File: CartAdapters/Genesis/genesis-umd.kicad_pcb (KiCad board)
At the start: 2 copper layers, 26.7 x 94.6 mm, 4 parts, among them CON101 UMDv2-CONN, CON102 GENESIS-CONN, U101 MCP23008T-E_SS

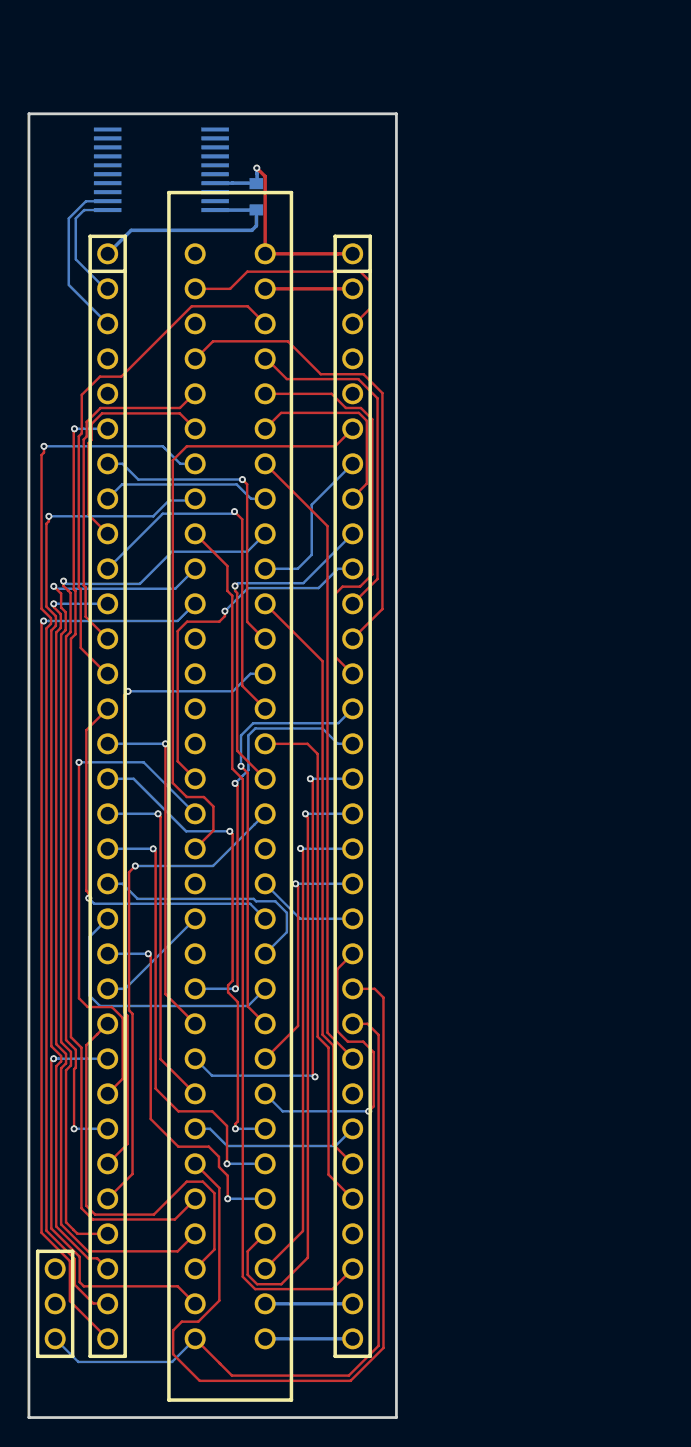
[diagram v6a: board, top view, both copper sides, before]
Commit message: ground plane added to genesis UMD adapter
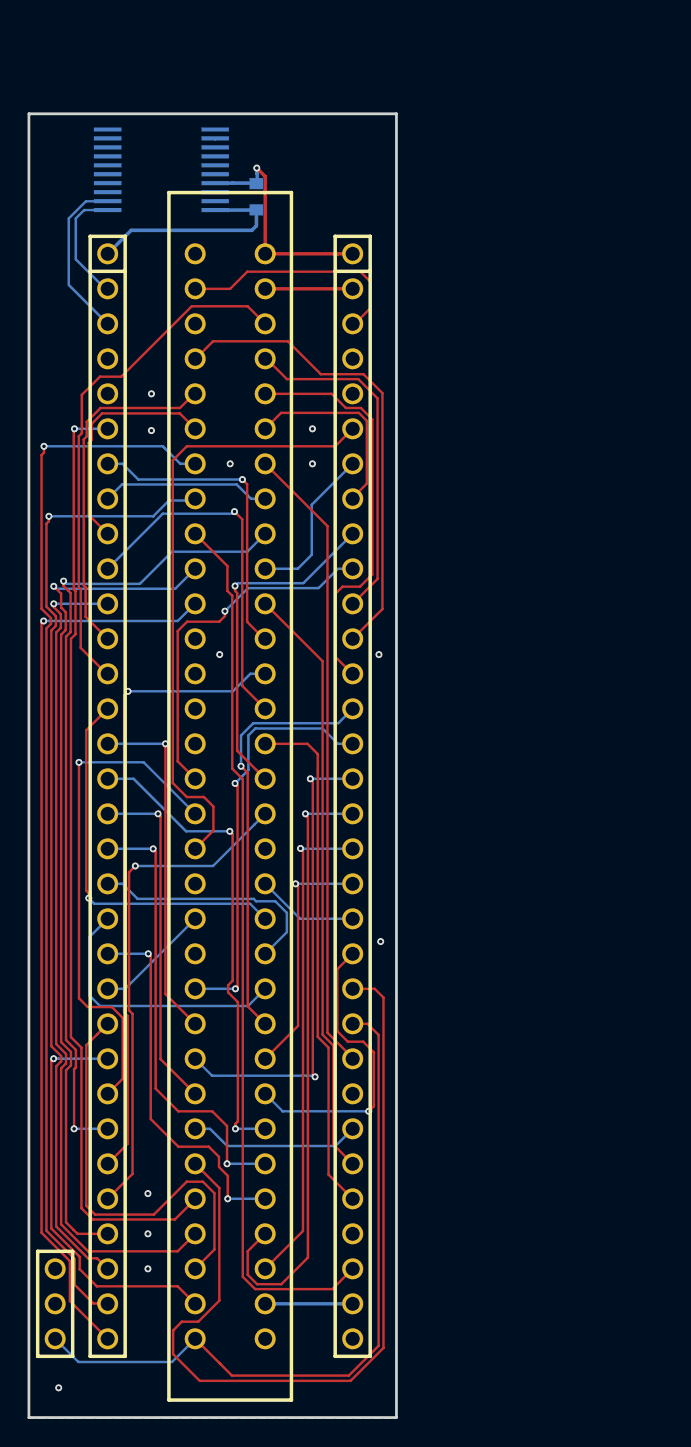
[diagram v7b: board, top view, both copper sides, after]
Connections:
- CON101 pad 33: /GND_1 -> GND
- CON102 pad A18: Net-(CON102-PadA18) -> GND
- CON102 pad A32: /GND_1 -> GND
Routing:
- net /GND_1: track 6.35 -> 0.00 mm
- net /~TIME~: track 30.1 -> 29.6 mm
- net GND: vias 1 -> 13
- added copper zone on B.Cu, net GND
- added copper zone on F.Cu, net GND
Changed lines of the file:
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@@
     (thickness 1.6)
     (drawings 4)
-    (tracks 489)
+    (tracks 501)
     (zones 0)
     (modules 4)
-    (nets 80)
+    (nets 78)
   )
   (page A4)
@@
     (35 F.Paste user)
     (36 B.SilkS user)
-    (37 F.SilkS user hide)
+    (37 F.SilkS user)
     (38 B.Mask user)
     (39 F.Mask user)
@@
     (last_trace_width 0.1778)
     (trace_clearance 0.1778)
-    (zone_clearance 0.508)
+    (zone_clearance 0.254)
     (zone_45_only no)
     (trace_min 0.1778)
@@
   (net 76 /5V_0)
   (net 77 /5V_1)
-  (net 78 /GND_1)
-  (net 79 "Net-(CON102-PadA18)")
   (net_class Default "This is the default net class."
     (clearance 0.1778)
@@
     (add_net /D8)
     (add_net /D9)
-    (add_net /GND_1)
     (add_net /SCL)
     (add_net /SDA)
@@
     (add_net "Net-(CON101-Pad65)")
     (add_net "Net-(CON101-Pad66)")
-    (add_net "Net-(CON102-PadA18)")
     (add_net "Net-(CON102-PadB1)")
     (add_net "Net-(CON102-PadB12)")
@@
       (net 77 /5V_1))
     (pad 33 thru_hole circle (at 17.78 78.74) (size 1.524 1.524) (drill 1.016) (layers *.Cu *.Mask)
-      (net 78 /GND_1))
+      (net 2 GND))
     (pad 32 thru_hole circle (at 0 78.74) (size 1.524 1.524) (drill 1.016) (layers *.Cu *.Mask)
       (net 29 /A23))
@@
       (net 46 /D1))
     (pad A32 thru_hole circle (at 5.08 78.74 180) (size 1.524 1.524) (drill 1.016) (layers *.Cu *.Mask)
-      (net 78 /GND_1))
+      (net 2 GND))
     (pad A31 thru_hole circle (at 5.08 76.2 180) (size 1.524 1.524) (drill 1.016) (layers *.Cu *.Mask)
       (net 77 /5V_1))
@@
       (net 25 /A1))
     (pad A18 thru_hole circle (at 5.08 43.18 180) (size 1.524 1.524) (drill 1.016) (layers *.Cu *.Mask)
-      (net 79 "Net-(CON102-PadA18)"))
+      (net 2 GND))
     (pad A19 thru_hole circle (at 5.08 45.72 180) (size 1.524 1.524) (drill 1.016) (layers *.Cu *.Mask)
       (net 40 /D7))
@@
   (segment (start 144.9498 60.9092) (end 146.6342 60.9092) (width 0.254) (layer B.Cu) (net 2))
   (segment (start 146.6342 60.9092) (end 146.6596 60.8838) (width 0.254) (layer B.Cu) (net 2))
-  (segment (start 147.32 144.78) (end 153.67 144.78) (width 0.254) (layer B.Cu) (net 78))
+  (segment (start 143.69 57.711) (end 143.6878 57.7088) (width 0.254) (layer B.Cu) (net 2))
+  (via (at 139.065 76.2) (size 0.508) (drill 0.254) (layers F.Cu B.Cu) (net 2))
+  (via (at 139.065 78.867) (size 0.508) (drill 0.254) (layers F.Cu B.Cu) (net 2))
+  (via (at 150.749 78.74) (size 0.508) (drill 0.254) (layers F.Cu B.Cu) (net 2))
+  (via (at 150.749 81.28) (size 0.508) (drill 0.254) (layers F.Cu B.Cu) (net 2))
+  (via (at 144.78 81.28) (size 0.508) (drill 0.254) (layers F.Cu B.Cu) (net 2))
+  (via (at 144.018 95.123) (size 0.508) (drill 0.254) (layers F.Cu B.Cu) (net 2))
+  (via (at 132.334 148.336) (size 0.508) (drill 0.254) (layers F.Cu B.Cu) (net 2))
+  (via (at 155.575 95.123) (size 0.508) (drill 0.254) (layers F.Cu B.Cu) (net 2))
+  (via (at 155.702 115.951) (size 0.508) (drill 0.254) (layers F.Cu B.Cu) (net 2))
+  (via (at 138.811 139.7) (size 0.508) (drill 0.254) (layers F.Cu B.Cu) (net 2))
+  (via (at 138.811 137.16) (size 0.508) (drill 0.254) (layers F.Cu B.Cu) (net 2))
+  (via (at 138.811 134.239) (size 0.508) (drill 0.254) (layers F.Cu B.Cu) (net 2))
   (segment (start 133.0706 68.3006) (end 133.0706 63.4746) (width 0.1778) (layer B.Cu) (net 3))
   (segment (start 135.89 71.12) (end 133.0706 68.3006) (width 0.1778) (layer B.Cu) (net 3))
@@
   (segment (start 147.32 81.28) (end 151.841222 85.801222) (width 0.1778) (layer F.Cu) (net 36))
   (segment (start 151.841222 122.565206) (end 153.67 124.393984) (width 0.1778) (layer F.Cu) (net 36))
-  (segment (start 147.32 68.58) (end 153.6954 68.58) (width 0.254) (layer F.Cu) (net 76))
-  (segment (start 147.32 142.24) (end 153.67 142.24) (width 0.254) (layer B.Cu) (net 77))
   (segment (start 154.74763 121.92) (end 155.5496 122.72197) (width 0.1778) (layer F.Cu) (net 37))
   (segment (start 153.67 121.92) (end 154.74763 121.92) (width 0.1778) (layer F.Cu) (net 37))
@@
   (segment (start 150.6982 87.884) (end 150.6982 84.2518) (width 0.1778) (layer B.Cu) (net 53))
   (via (at 131.968449 124.449846) (size 0.508) (drill 0.254) (layers F.Cu B.Cu) (net 54))
-  (segment (start 142.24 142.24) (end 140.97 140.97) (width 0.1778) (layer F.Cu) (net 54))
   (segment (start 132.327659 124.449846) (end 131.968449 124.449846) (width 0.1778) (layer B.Cu) (net 54))
-  (segment (start 131.800589 124.617706) (end 131.968449 124.449846) (width 0.1778) (layer F.Cu) (net 54))
-  (segment (start 140.97 140.97) (end 134.1628 140.97) (width 0.1778) (layer F.Cu) (net 54))
-  (segment (start 134.1628 140.97) (end 133.857998 140.665198) (width 0.1778) (layer F.Cu) (net 54))
-  (segment (start 131.800589 136.773898) (end 131.800589 124.617706) (width 0.1778) (layer F.Cu) (net 54))
-  (segment (start 133.857998 140.665198) (end 133.857998 138.831306) (width 0.1778) (layer F.Cu) (net 54))
   (segment (start 135.905246 124.449846) (end 132.327659 124.449846) (width 0.1778) (layer B.Cu) (net 54))
   (segment (start 135.9154 124.46) (end 135.905246 124.449846) (width 0.1778) (layer B.Cu) (net 54))
+  (segment (start 142.24 142.24) (end 140.97 140.97) (width 0.1778) (layer F.Cu) (net 54))
+  (segment (start 140.97 140.97) (end 135.102598 140.97) (width 0.1778) (layer F.Cu) (net 54))
+  (segment (start 135.102598 140.97) (end 133.857998 139.7254) (width 0.1778) (layer F.Cu) (net 54))
+  (segment (start 133.857998 139.7254) (end 133.857998 138.831306) (width 0.1778) (layer F.Cu) (net 54))
   (segment (start 133.857998 138.831306) (end 131.800589 136.773898) (width 0.1778) (layer F.Cu) (net 54))
+  (segment (start 131.800589 124.617706) (end 131.968449 124.449846) (width 0.1778) (layer F.Cu) (net 54))
+  (segment (start 131.800589 136.773898) (end 131.800589 124.617706) (width 0.1778) (layer F.Cu) (net 54))
   (segment (start 142.24 68.58) (end 144.78 68.58) (width 0.1778) (layer F.Cu) (net 57))
   (segment (start 144.78 68.58) (end 146.0246 67.3354) (width 0.1778) (layer F.Cu) (net 57))
@@
   (segment (start 134.9756 135.763) (end 134.3406 135.128) (width 0.1778) (layer F.Cu) (net 74))
   (segment (start 141.6304 133.3754) (end 139.2428 135.763) (width 0.1778) (layer F.Cu) (net 74))
+  (segment (start 147.32 68.58) (end 153.6954 68.58) (width 0.254) (layer F.Cu) (net 76))
+  (segment (start 147.32 142.24) (end 153.67 142.24) (width 0.254) (layer B.Cu) (net 77))
   (zone (net 0) (net_name "") (layers F&B.Cu) (hatch edge 0.508)
     (connect_pads (clearance 0.508))
@@
       )
     )
+  )
+  (zone (net 2) (net_name GND) (layer B.Cu) (hatch edge 0.508)
+    (connect_pads (clearance 0.254))
+    (min_thickness 0.1778)
+    (fill yes (arc_segments 16) (thermal_gap 0.254) (thermal_bridge_width 0.254))
+    (polygon
+      (pts
+        (xy 130.175 55.88) (xy 130.175 150.495) (xy 156.845 150.495) (xy 156.845 55.88)
+      )
+    )
+  )
+  (zone (net 2) (net_name GND) (layer F.Cu) (hatch edge 0.508)
+    (connect_pads (clearance 0.254))
+    (min_thickness 0.1778)
+    (fill yes (arc_segments 16) (thermal_gap 0.254) (thermal_bridge_width 0.254))
+    (polygon
+      (pts
+        (xy 130.175 55.88) (xy 130.175 150.495) (xy 156.845 150.495) (xy 156.845 55.88)
+      )
+    )

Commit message: changed Genesis CE to CE3
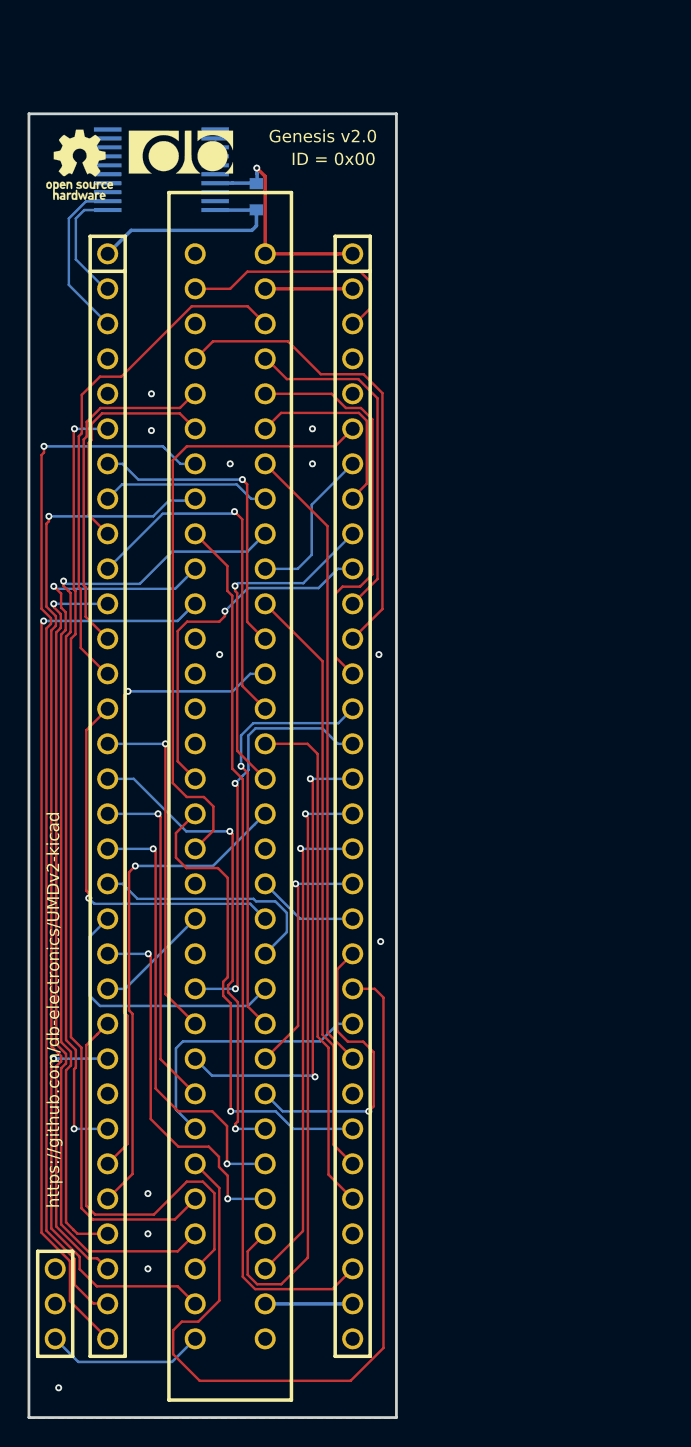
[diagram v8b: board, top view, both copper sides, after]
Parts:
- added G***: LOGO, db-artwork:db-logo_7.5mm, F.Cu at (141.2, 58.7)
- added G***: LOGO, db-artwork:oshw-logo_5mm, F.Cu at (133.9, 59.6)
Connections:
- CON101 pad 25: /~CE~ -> (no net)
- CON101 pad 36: /A0 -> (no net)
- CON101 pad 39: /~ASEL~ -> /~CE~
- CON101 pad 4: Net-(CON101-Pad4) -> (no net)
- CON101 pad 40: Net-(CON101-Pad40) -> (no net)
- CON101 pad 42: Net-(CON101-Pad42) -> /~ASEL~
- CON101 pad 5: Net-(CON101-Pad5) -> (no net)
- CON101 pad 60: Net-(CON101-Pad60) -> (no net)
- CON101 pad 61: Net-(CON101-Pad61) -> (no net)
- CON101 pad 65: Net-(CON101-Pad65) -> (no net)
- CON101 pad 66: Net-(CON101-Pad66) -> (no net)
- CON102 pad B1: Net-(CON102-PadB1) -> (no net)
- CON102 pad B12: Net-(CON102-PadB12) -> (no net)
- CON102 pad B13: Net-(CON102-PadB13) -> (no net)
- CON102 pad B14: Net-(CON102-PadB14) -> (no net)
- CON102 pad B15: Net-(CON102-PadB15) -> (no net)
- CON102 pad B19: Net-(CON102-PadB19) -> (no net)
- CON102 pad B21: Net-(CON102-PadB21) -> (no net)
- CON102 pad B3: Net-(CON102-PadB3) -> (no net)
- U101 pad 10: Net-(U101-Pad10) -> (no net)
- U101 pad 11: Net-(U101-Pad11) -> (no net)
- U101 pad 7: Net-(U101-Pad7) -> (no net)
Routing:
- net /~CART~: track 51.7 -> 11.5 mm
- net /~ASEL~: track 12.5 -> 20.0 mm
- net /~CE~: track 36.8 -> 34.9 mm
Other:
- board text added: "Genesis v2.0"
- board text added: "ID = 0x00"
- board text added: "https://github.com/db-electronics/UMDv2-kicad"
